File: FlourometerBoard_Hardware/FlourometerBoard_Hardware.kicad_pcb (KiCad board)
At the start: 2 copper layers, 12 parts, among them J1 RJ45_LED_Shielded, U1 Teensy4.1_DEV-16771, U3 OKI

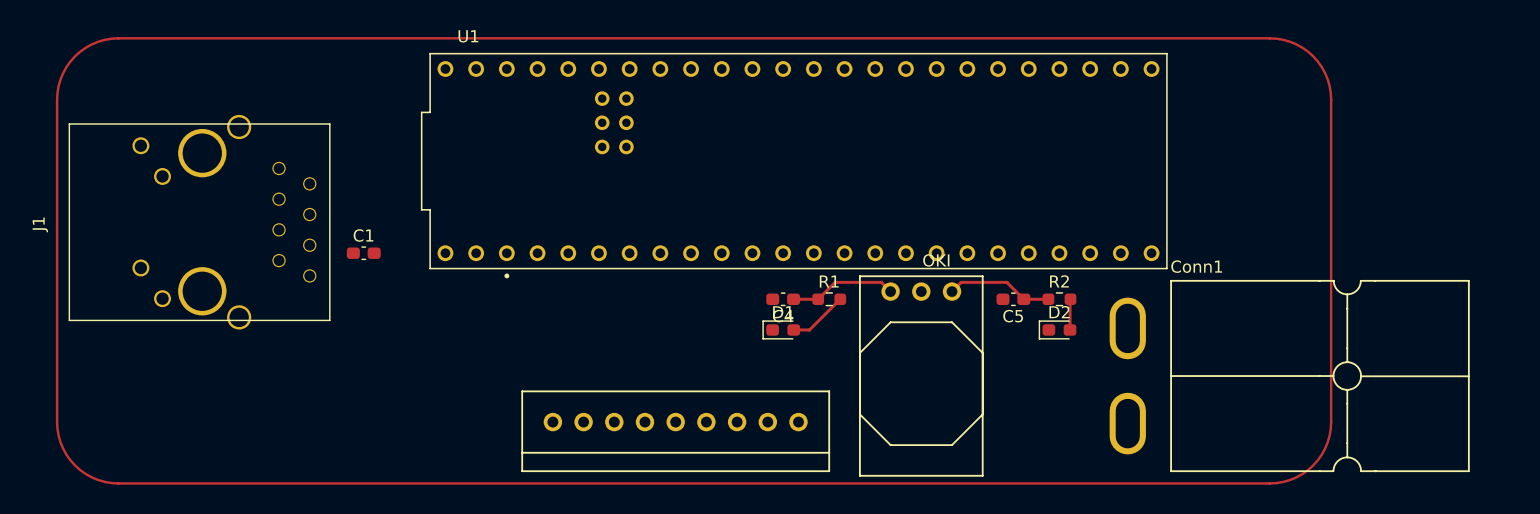
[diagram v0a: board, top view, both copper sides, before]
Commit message: Finished routing all traces on layout
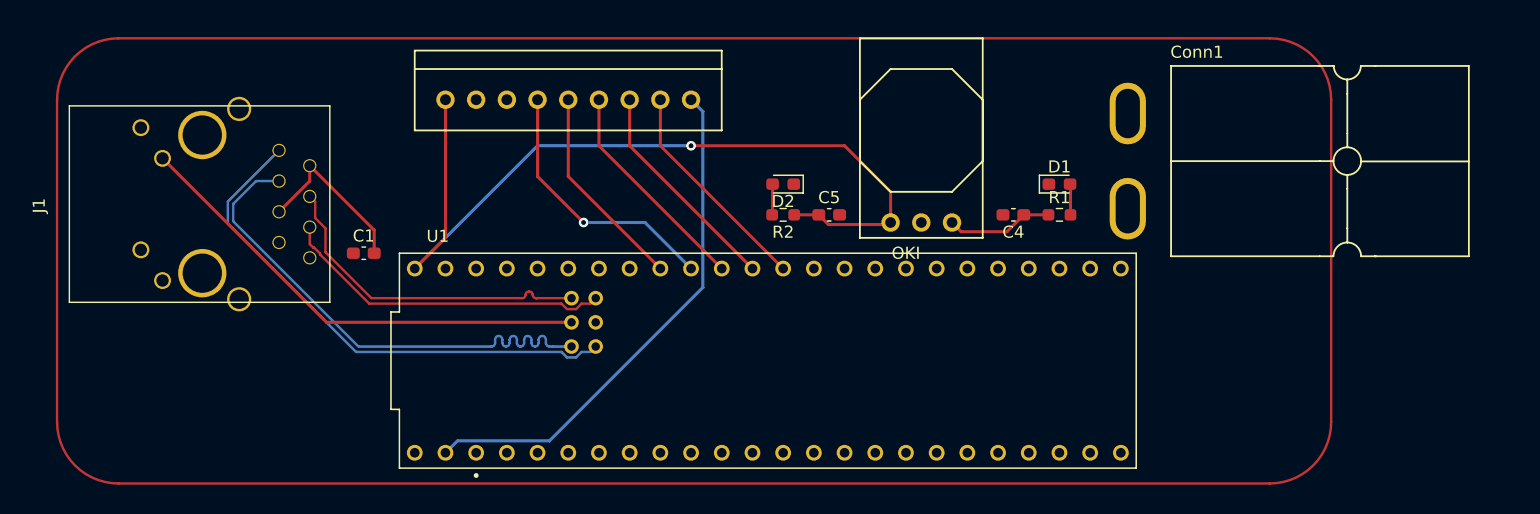
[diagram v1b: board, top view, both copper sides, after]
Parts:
- moved Conn2 39.6 mm to (71.1, 86.4), turned to 0 degrees
- moved D1 25.8 mm to (121.9, 93.3)
- moved D2 25.8 mm to (99.1, 93.3), turned to 180 degrees
- moved R2 23.9 mm to (99.1, 95.9), turned to 180 degrees
- moved C4 20.3 mm to (118.1, 95.9)
- moved R1 20.3 mm to (121.9, 95.9)
- moved Conn1 17.8 mm to (127.4, 95.7)
- moved C5 16.8 mm to (102.9, 95.9), turned to 0 degrees
- moved U1 16.7 mm to (97.8, 108.0)
- moved U3 7.65 mm to (113.0, 96.5), turned to 180 degrees
- moved J1 1.50 mm to (38.0, 95.1)
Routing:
- net +3V3: track 8.87 -> 71.1 mm, vias 0 -> 1
- net T+: track 0.00 -> 43.2 mm
- net T-: track 0.00 -> 43.0 mm
- net WHITE_LED: track 0.00 -> 42.9 mm
- net LED: track 0.00 -> 39.5 mm
- net R-: track 0.00 -> 27.7 mm
- net R+: track 0.00 -> 27.7 mm
- net EOS: track 0.00 -> 22.2 mm, vias 0 -> 1
- net START: track 0.00 -> 18.2 mm
- net VIDEO: track 0.00 -> 18.2 mm
- net CLK: track 0.00 -> 18.2 mm
- net TRG: track 0.00 -> 17.1 mm
- net Net-(C1-Pad2): track 0.00 -> 14.3 mm
- net Net-(D1-A): track 4.90 -> 2.56 mm

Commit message: Initial Fluoro Board Layout Complete
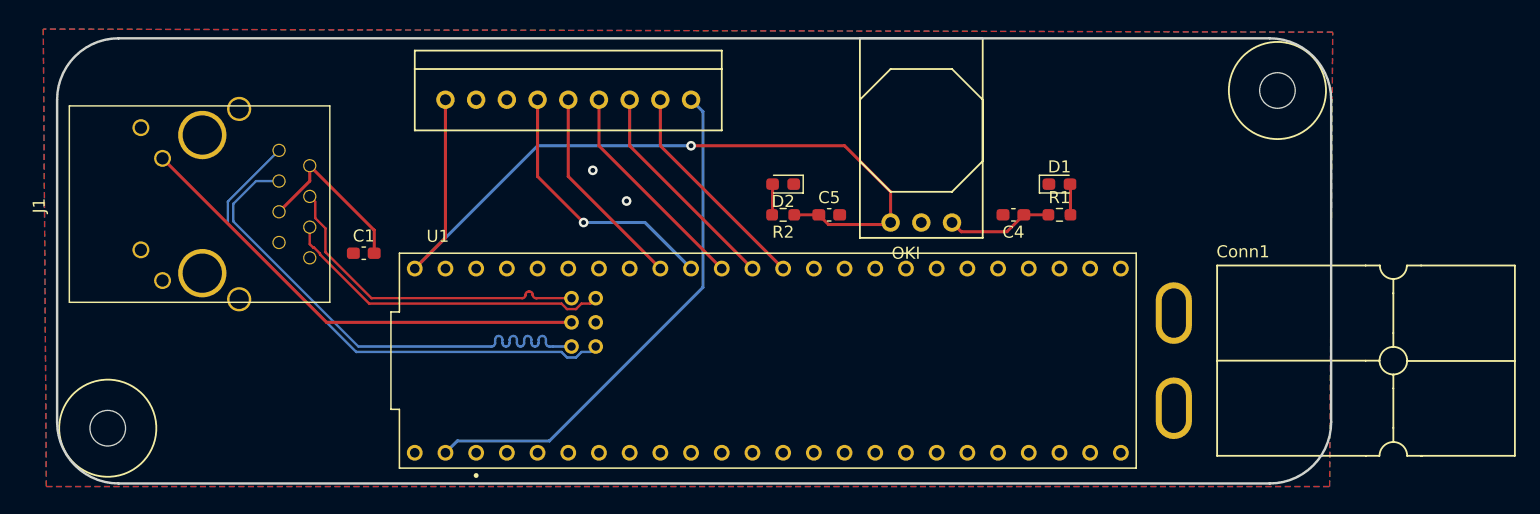
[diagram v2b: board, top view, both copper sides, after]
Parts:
- added REF**: 4_40_Hole, MRDT_Drill_Holes:4_40_Hole, F.Cu at (140.0, 85.6)
- added REF**: 4_40_Hole, MRDT_Drill_Holes:4_40_Hole, F.Cu at (43.2, 113.5)
- moved Conn1 16.9 mm to (131.3, 112.2)
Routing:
- net GND: vias 0 -> 2
- added copper zone on B.Cu, net GND
- added copper zone on F.Cu, net GND
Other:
- board outline added: 105.4 x 36.8 mm
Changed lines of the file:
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@@
     )
+  )
+  (footprint "MRDT_Drill_Holes:4_40_Hole" (layer "F.Cu")
+    (at 139.954 85.598)
+    (clearance 2.54)
+    (attr through_hole)
+    (fp_text reference "REF**" (at -0.00508 0.50508) (layer "F.SilkS") hide
+        (effects (font (size 1 1) (thickness 0.15)))
+    )
+    (fp_text value "4_40_Hole" (at -0.00508 -0.49492) (layer "F.Fab") hide
+        (effects (font (size 1 1) (thickness 0.15)))
+    )
+    (fp_circle (center 0 0) (end -0.00508 4.01828)
+      (stroke (width 0.15) (type solid)) (fill none) (layer "F.SilkS"))
+    (pad "" np_thru_hole circle (at 0 0) (size 2.9464 2.9464) (drill 2.9464) (layers "*.Cu" "*.Mask")
+      (clearance 2.5))
   )
   (footprint "MRDT_Connectors:Square_Anderson_2_H_Side_By_Side_PV" (layer "F.Cu")
-    (at 127.4482 95.677 180)
+    (at 131.2582 112.187 180)
     (property "Sheetfile" "FlourometerBoard_Hardware.kicad_sch")
     (property "Sheetname" "")
@@
       (rotate (xyz 0 0 0))
     )
+  )
+  (footprint "MRDT_Drill_Holes:4_40_Hole" (layer "F.Cu")
+    (at 43.18 113.538)
+    (clearance 2.54)
+    (attr through_hole)
+    (fp_text reference "REF**" (at -0.00508 0.50508) (layer "F.SilkS") hide
+        (effects (font (size 1 1) (thickness 0.15)))
+    )
+    (fp_text value "4_40_Hole" (at -0.00508 -0.49492) (layer "F.Fab") hide
+        (effects (font (size 1 1) (thickness 0.15)))
+    )
+    (fp_circle (center 0 0) (end -0.00508 4.01828)
+      (stroke (width 0.15) (type solid)) (fill none) (layer "F.SilkS"))
+    (pad "" np_thru_hole circle (at 0 0) (size 2.9464 2.9464) (drill 2.9464) (layers "*.Cu" "*.Mask")
+      (clearance 2.5))
   )
   (footprint "MRDT_Connectors:RJ45_Teensy" (layer "F.Cu")
@@
   )
   (gr_arc (start 38.989 86.36) (mid 40.476898 82.767898) (end 44.069 81.28)
-    (stroke (width 0.2) (type default)) (layer "F.Cu"))
+    (stroke (width 0.2) (type default)) (layer "Edge.Cuts"))
   (gr_line (start 144.399 86.36) (end 144.399 113.03)
-    (stroke (width 0.2) (type default)) (layer "F.Cu"))
+    (stroke (width 0.2) (type default)) (layer "Edge.Cuts"))
   (gr_line (start 38.989 86.36) (end 38.989 113.03)
-    (stroke (width 0.2) (type default)) (layer "F.Cu"))
+    (stroke (width 0.2) (type default)) (layer "Edge.Cuts"))
   (gr_line (start 44.069 81.28) (end 139.319 81.28)
-    (stroke (width 0.2) (type default)) (layer "F.Cu"))
+    (stroke (width 0.2) (type default)) (layer "Edge.Cuts"))
   (gr_arc (start 44.069 118.11) (mid 40.476898 116.622102) (end 38.989 113.03)
-    (stroke (width 0.2) (type default)) (layer "F.Cu"))
+    (stroke (width 0.2) (type default)) (layer "Edge.Cuts"))
   (gr_line (start 44.069 118.11) (end 139.319 118.11)
-    (stroke (width 0.2) (type default)) (layer "F.Cu"))
+    (stroke (width 0.2) (type default)) (layer "Edge.Cuts"))
   (gr_arc (start 139.319 81.28) (mid 142.911102 82.767898) (end 144.399 86.36)
-    (stroke (width 0.2) (type default)) (layer "F.Cu"))
+    (stroke (width 0.2) (type default)) (layer "Edge.Cuts"))
   (gr_arc (start 144.399 113.03) (mid 142.911102 116.622102) (end 139.319 118.11)
-    (stroke (width 0.2) (type default)) (layer "F.Cu"))
+    (stroke (width 0.2) (type default)) (layer "Edge.Cuts"))
+  (via (at 83.312 92.202) (size 0.8) (drill 0.4) (layers "F.Cu" "B.Cu") (free) (net 1))
+  (via (at 86.106 94.742) (size 0.8) (drill 0.4) (layers "F.Cu" "B.Cu") (free) (net 1))
   (segment (start 59.8925 93.091) (end 57.3525 95.631) (width 0.254) (layer "F.Cu") (net 2))
   (segment (start 65.225 97.1535) (end 59.8925 91.821) (width 0.254) (layer "F.Cu") (net 2))
@@
   (segment (start 82.37845 103.23) (end 83.1 103.23) (width 0.2) (layer "F.Cu") (net 20))
   (segment (start 60.1728 98.591) (end 60.244582 98.591) (width 0.2) (layer "F.Cu") (net 20))
-  (group "" (id 25181b0e-30dd-423e-a917-bd13f34ce9f0)
+  (zone (net 1) (net_name "GND") (layer "F.Cu") (hatch edge 0.5)
+    (connect_pads (clearance 0.5))
+    (min_thickness 0.25) (filled_areas_thickness no)
+    (fill yes (thermal_gap 0.5) (thermal_bridge_width 0.5))
+    (polygon
+      (pts
+        (xy 37.846 80.518)
+        (xy 38.1 118.364)
+        (xy 144.272 118.364)
+        (xy 144.526 80.772)
+      )
+    )
+  )
+  (zone (net 1) (net_name "GND") (layer "B.Cu") (hatch edge 0.5)
+    (priority 1)
+    (connect_pads (clearance 0.5))
+    (min_thickness 0.25) (filled_areas_thickness no)
+    (fill yes (thermal_gap 0.5) (thermal_bridge_width 0.5))
+    (polygon
+      (pts
+        (xy 144.272 118.364)
+        (xy 144.526 80.772)
+        (xy 37.846 80.518)
+        (xy 38.1 118.364)
+      )
+    )
+  )
+  (group "" (id e602fc76-7f28-4c87-9158-1bb29df57a39)
     (members
       38641a9d-d20d-4218-bbe5-bb54ee73d7af
